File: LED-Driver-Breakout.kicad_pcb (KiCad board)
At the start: 6 copper layers, 120.9 x 67.1 mm, 16 parts, among them U1 V10P45-M3/86A, U2 TSR2-24120

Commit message: updates based on suggestions
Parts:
- added C3: 10µf, Capacitor_SMD:C_0805_2012Metric, F.Cu at (105.8, 109.2)
- added C4: 10µF, Capacitor_SMD:C_0805_2012Metric, F.Cu at (103.0, 109.2)
- added C5: 10µF, Capacitor_SMD:C_0805_2012Metric, F.Cu at (99.8, 109.5)
- added C6: 56µF, Capacitor_SMD:CP_Elec_8x10, F.Cu at (89.0, 112.2)
- added L1: 5.6µH, Inductor_SMD:L_0805_2012Metric_Pad1.05x1.20mm_HandSolder, F.Cu at (99.8, 112.2)
- moved U2 9.57 mm to (102.2, 118.8), turned to 0 degrees
- moved   1.40 mm to (100.6, 102.7)
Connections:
-   pad 1: V_Fused -> VRegulated
- PS1 pad 3: unconnected-(PS1-DIM--Pad3) -> GND
- PS1 pad 5: Switch pin -> Switch
- U2 pad 1: V_Fused -> Net-(U2-Vin)
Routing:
- net V_Fused: track 0.00 -> 41.6 mm, vias 6 -> 3
- net GND: track 0.00 -> 34.1 mm, vias 3 -> 4
- net Net-(U2-Vin): track 0.00 -> 23.5 mm
- net +BATT: track 23.0 -> 19.0 mm
- net (no net): track 0.00 -> 0.51 mm

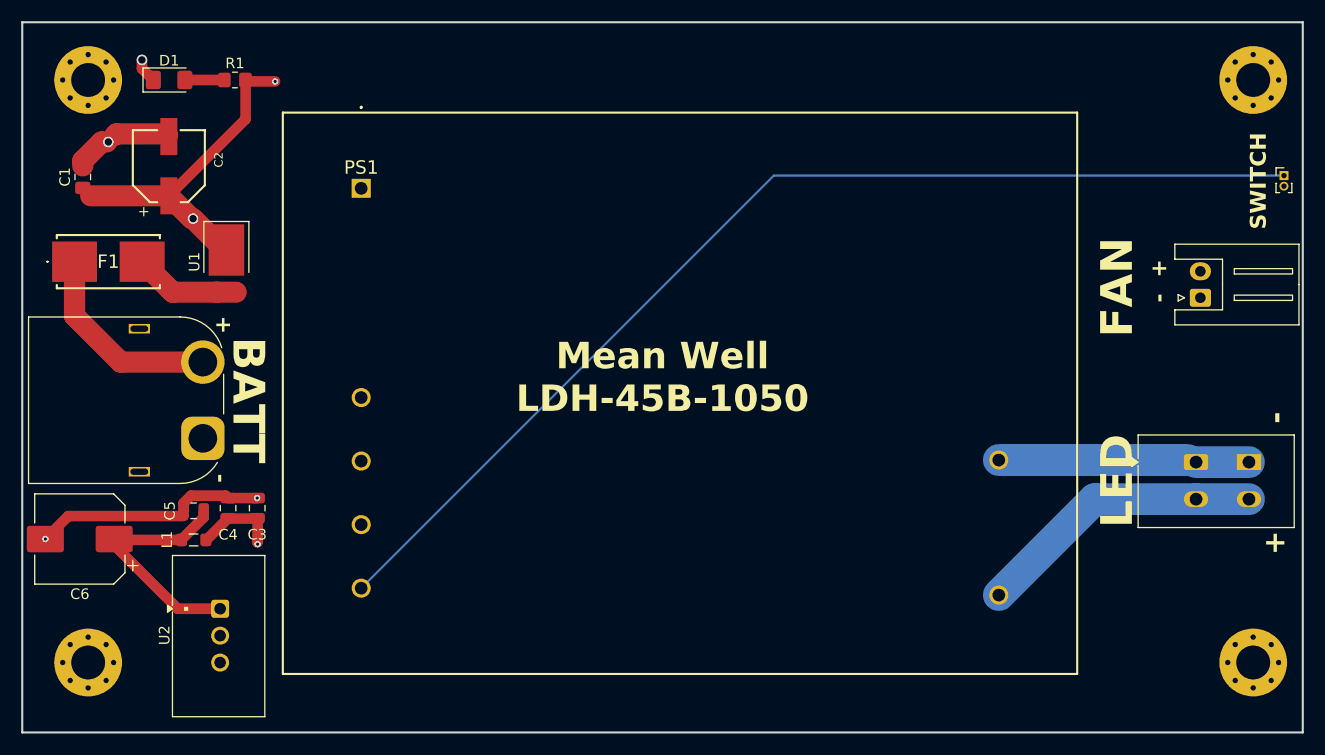
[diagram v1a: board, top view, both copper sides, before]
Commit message: finished pcb routing may need to make the board more square
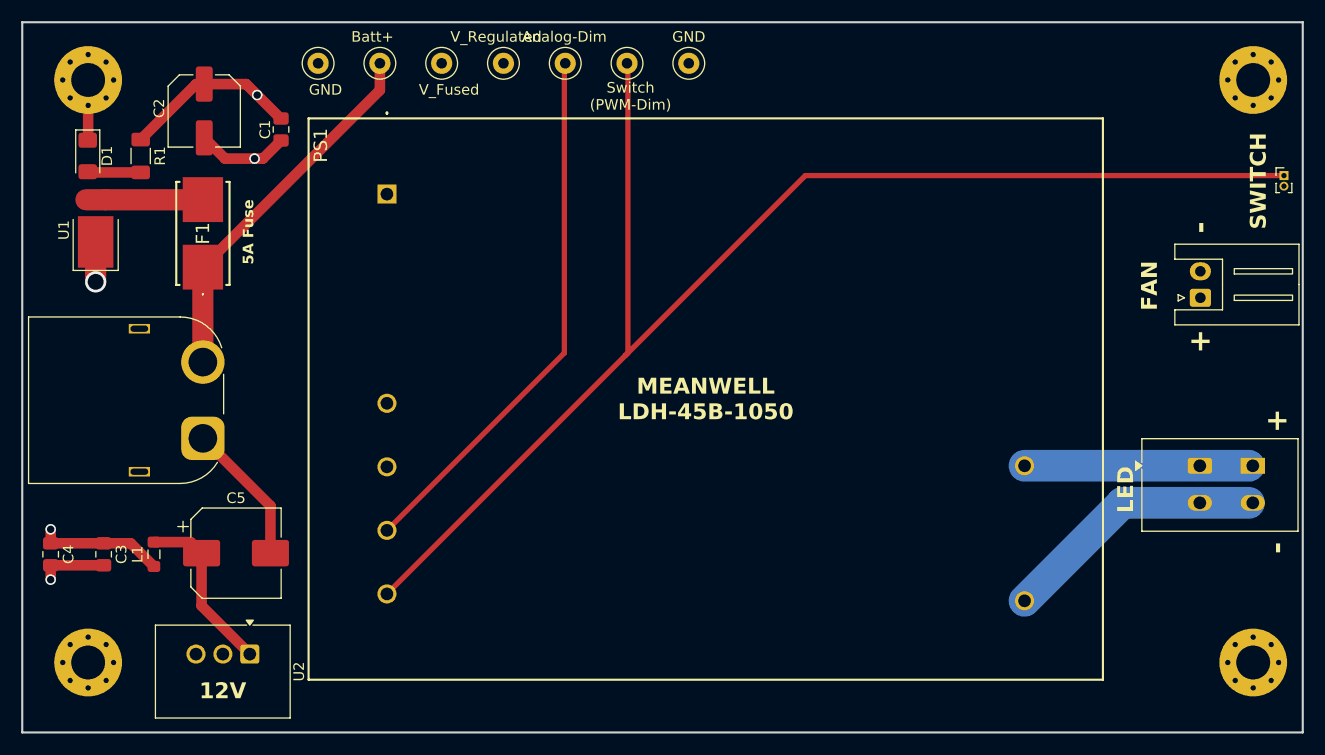
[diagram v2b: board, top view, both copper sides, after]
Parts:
- removed C6: 56µF, Capacitor_SMD:CP_Elec_8x10
- added Analog-Dim: TestPoint_Loop_D1.80mm_Drill1.0mm_Beaded, TestPoint:TestPoint_Loop_D1.80mm_Drill1.0mm_Beaded, F.Cu at (134.8, 67.2)
- added Batt+: TestPoint_Loop_D1.80mm_Drill1.0mm_Beaded, TestPoint:TestPoint_Loop_D1.80mm_Drill1.0mm_Beaded, F.Cu at (117.3, 67.2)
- added GND: TestPoint_Loop_D1.80mm_Drill1.0mm_Beaded, TestPoint:TestPoint_Loop_D1.80mm_Drill1.0mm_Beaded, F.Cu at (111.5, 67.2)
- added GND: TestPoint_Loop_D1.80mm_Drill1.0mm_Beaded, TestPoint:TestPoint_Loop_D1.80mm_Drill1.0mm_Beaded, F.Cu at (146.5, 67.2)
- added Switch(PWM-Dim): TestPoint_Loop_D1.80mm_Drill1.0mm_Beaded, TestPoint:TestPoint_Loop_D1.80mm_Drill1.0mm_Beaded, F.Cu at (140.7, 67.2)
- added V_Fused: TestPoint_Loop_D1.80mm_Drill1.0mm_Beaded, TestPoint:TestPoint_Loop_D1.80mm_Drill1.0mm_Beaded, F.Cu at (123.2, 67.2)
- added V_Regulated: TestPoint_Loop_D1.80mm_Drill1.0mm_Beaded, TestPoint:TestPoint_Loop_D1.80mm_Drill1.0mm_Beaded, F.Cu at (129.0, 67.2)
- C2: footprint 865080645012:WCAP-ASLI_6.3X7.7_DXL_ -> Capacitor_SMD:C_Elec_6.3x7.7
- C3: value 10µf -> 10 µF; footprint Capacitor_SMD:C_0805_2012Metric -> Capacitor_SMD:C_0805_2012Metric_Pad1.18x1.45mm_HandSolder
- C4: value 10µF -> 10 µF; footprint Capacitor_SMD:C_0805_2012Metric -> Capacitor_SMD:C_0805_2012Metric_Pad1.18x1.45mm_HandSolder
- C5: value 10µF -> 56 µF; footprint Capacitor_SMD:C_0805_2012Metric -> Capacitor_SMD:CP_Elec_8x10
- L1: value 5.6µH -> 5.6 µH
- R1: value 4.7 k -> 33K; footprint Resistor_SMD:R_0805_2012Metric_Pad1.20x1.40mm_HandSolder -> Resistor_SMD:R_1206_3216Metric_Pad1.30x1.75mm_HandSolder
- U2: value TSR2-24120 -> TSR0.5-2418; footprint Converter_DCDC:Converter_DCDC_TRACO_TSR2-xxxx_THT -> Converter_DCDC:Converter_DCDC_TRACO_TSR0.5-24xx_TSR0.5-24xxx_THT
- moved C1 19.2 mm to (108.0, 73.5), turned to -90 degrees
- moved C4 17.3 mm to (86.2, 113.6)
- moved C3 15.1 mm to (91.2, 113.6), turned to -90 degrees
- moved U1 12.7 mm to (90.5, 83.0), turned to 90 degrees
- moved R1 11.4 mm to (94.8, 76.0), turned to -90 degrees
- moved D1 10.5 mm to (89.8, 76.0), turned to -90 degrees
- moved F1 9.32 mm to (100.6, 83.3), turned to 90 degrees
- moved C2 6.19 mm to (100.8, 71.8)
- moved C5 5.66 mm to (103.8, 113.5), turned to 0 degrees
- moved U2 5.11 mm to (105.0, 123.0), turned to -90 degrees
- moved L1 3.99 mm to (96.0, 113.6), turned to 90 degrees
- moved PS1 2.49 mm to (118.0, 79.6)
- moved REF** 0.50 mm to (194.8, 105.2)
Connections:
- C4 pad 1: GND -> V_Fused
- C4 pad 2: V_Fused -> GND
- PS1 pad 5: Switch -> /switch
- REF** pad 1: Switch pin -> /switch
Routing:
- net /switch: track 0.00 -> 128.9 mm
- net Switch pin: track 103.3 -> 0.00 mm
- net unconnected-(PS1-ANALOG_DIM-Pad4): track 0.00 -> 51.1 mm
- net +BATT: track 19.0 -> 35.6 mm
- net V_Fused: track 41.6 -> 32.5 mm
- net Net-(U2-Vin): track 23.5 -> 16.3 mm
- net VOUT+: track 23.7 -> 21.2 mm
- net VOUT-: track 27.4 -> 25.0 mm
- net Net-(D1-A): track 3.73 -> 5.03 mm
- net Net-(F1-Pad2): track 10.1 -> 11.0 mm
- net (no net): track 0.51 -> 0.00 mm
- net GND: track 34.1 -> 34.3 mm, vias 4 -> 2
- added copper zone on In1.Cu, net GND
- removed copper zone on In1.Cu, net (none)
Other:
- board text added: "12V"
- board text added: "FAN"
- board text added: "MEANWELL LDH-45B-1050"
- board text added: "Switch (PWM-Dim)"
- board text removed: "."
- board text removed: "BATT"
- board text removed: "Mean Well LDH-45B-1050"

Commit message: forgot to save from last commit
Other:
- board text added: "45W LED Driver Breakout"

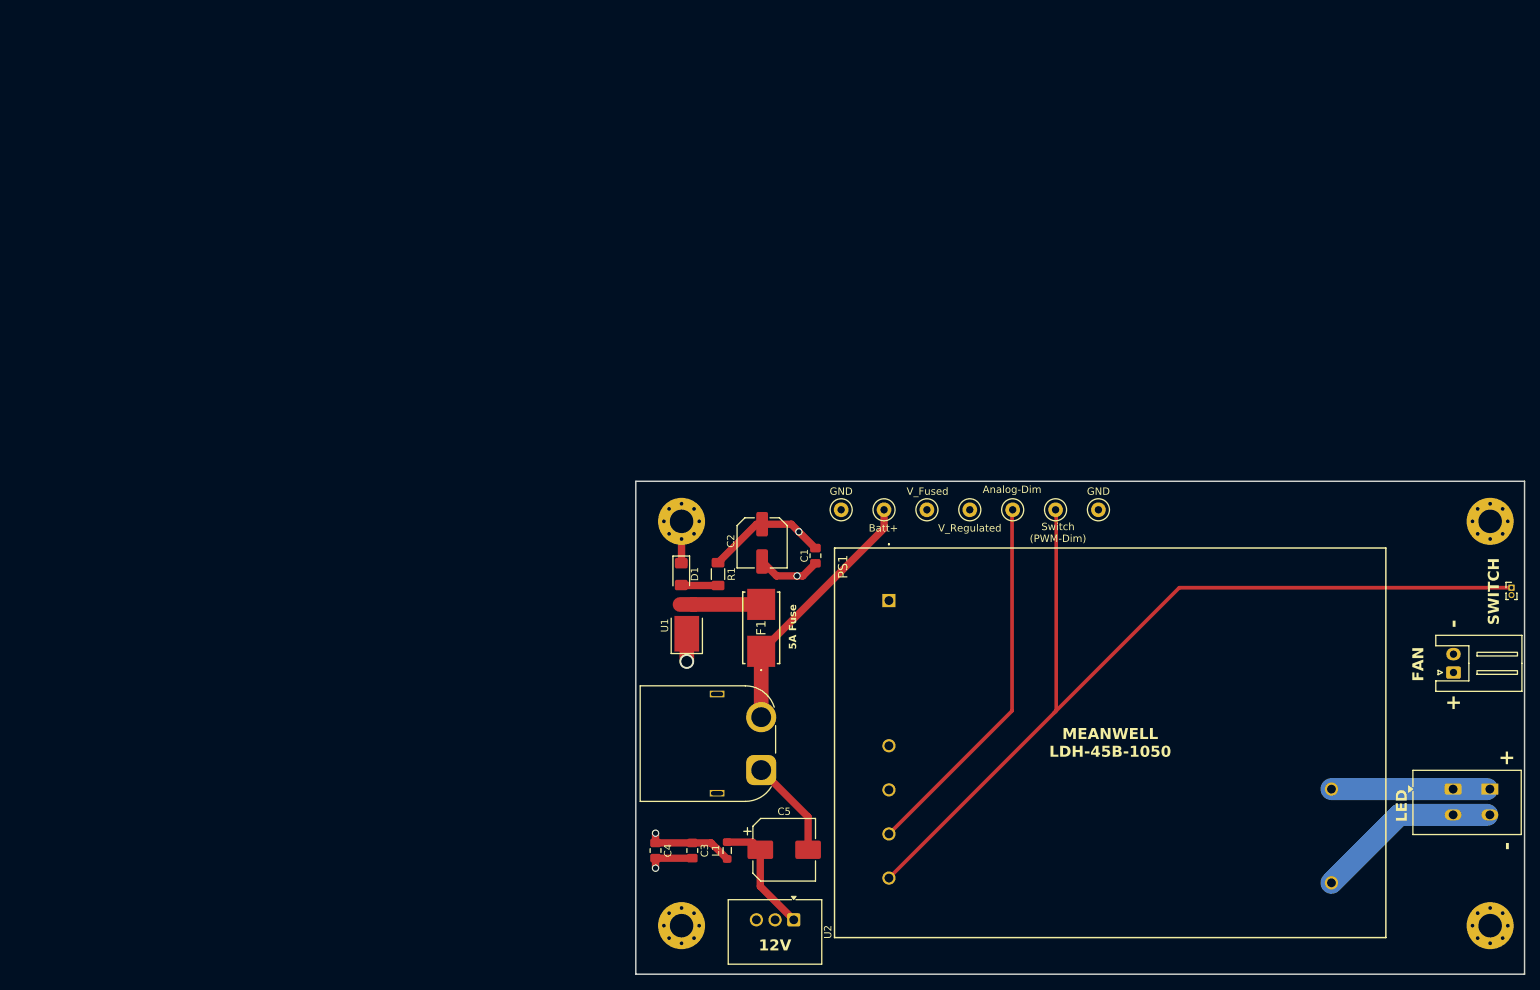
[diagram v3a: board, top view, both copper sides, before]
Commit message: made board square only need to add graphics
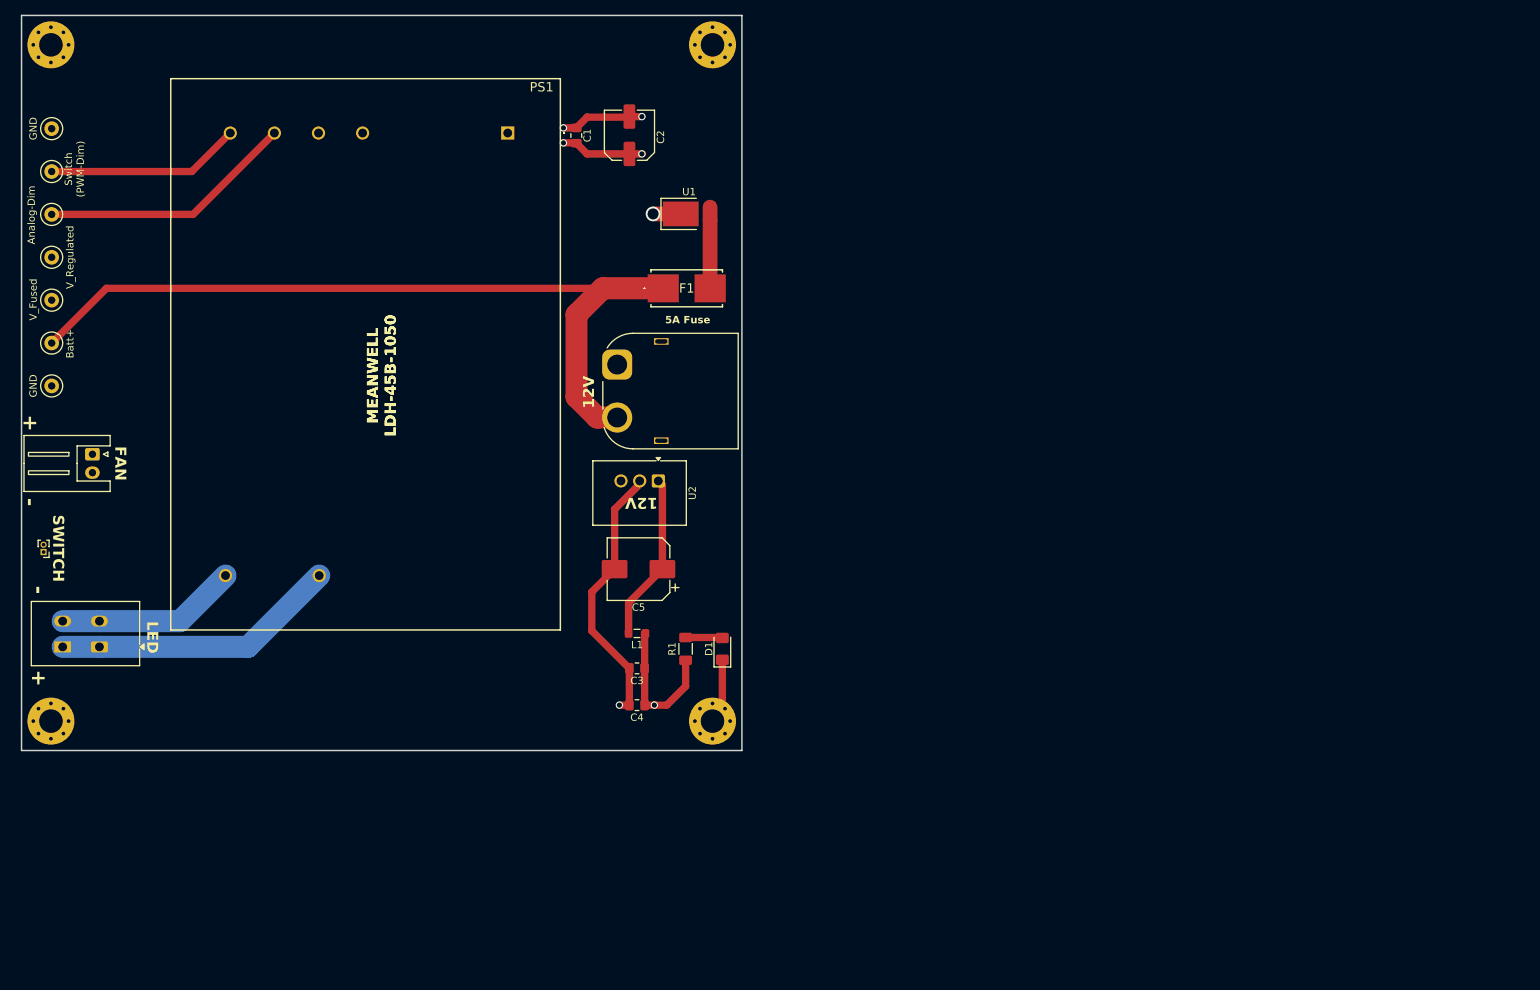
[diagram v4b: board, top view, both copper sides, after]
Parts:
- moved REF** 199.8 mm to (3.00, 73.0), turned to 180 degrees
- moved   187.5 mm to (9.64, 59.7), turned to -90 degrees
- moved REF** 185.2 mm to (10.6, 85.9), turned to 90 degrees
- moved GND 151.5 mm to (4.10, 15.4), turned to 90 degrees
- moved Switch(PWM-Dim) 144.1 mm to (4.10, 21.2), turned to 90 degrees
- moved Analog-Dim 136.8 mm to (4.10, 27.1), turned to -90 degrees
- moved V_Regulated 129.5 mm to (4.10, 32.9), turned to -90 degrees
- moved   124.1 mm to (94.0, 4.00)
- moved V_Fused 122.4 mm to (4.10, 38.7), turned to 90 degrees
- moved Batt+ 115.5 mm to (4.10, 44.6), turned to -90 degrees
- moved   109.4 mm to (94.0, 96.0)
- moved GND 108.7 mm to (4.10, 50.4), turned to 90 degrees
- moved   107.5 mm to (4.00, 4.00)
- moved   90.2 mm to (4.00, 96.0)
- moved PS1 82.1 mm to (66.2, 16.0), turned to 180 degrees
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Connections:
- REF** pad 1: /switch -> (no net)
- REF** pad 2: GND -> (no net)
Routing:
- net /switch: track 128.9 -> 26.8 mm
- net +BATT: track 35.6 -> 117.5 mm
- net GND: track 34.3 -> 57.1 mm, vias 2 -> 3
- net VOUT+: track 21.2 -> 38.9 mm
- net unconnected-(PS1-ANALOG_DIM-Pad4): track 51.1 -> 35.0 mm
- net Net-(U2-Vin): track 16.3 -> 22.9 mm
- net V_Fused: track 32.5 -> 35.1 mm, vias 3 -> 4
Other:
- board size 120.9 x 67.1 mm -> 98 x 100 mm

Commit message: forgot to add switch trace
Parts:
- moved U2 84.0 mm to (154.7, 112.5)
- moved   83.8 mm to (77.5, 108.8)
- moved Analog-Dim 83.5 mm to (71.6, 76.3)
- moved D1 83.5 mm to (162.9, 135.4)
- moved R1 83.5 mm to (157.9, 135.4)
- moved Switch(PWM-Dim) 83.5 mm to (71.6, 70.4)
- moved V_Fused 83.5 mm to (71.6, 87.9)
- moved   83.5 mm to (161.5, 53.2)
- moved   83.5 mm to (161.5, 145.2)
- moved Batt+ 83.5 mm to (71.6, 93.8)
- moved C1 83.5 mm to (143.0, 65.5)
- moved C5 83.5 mm to (151.5, 124.5)
- moved GND 83.5 mm to (71.6, 99.6)
- moved GND 83.5 mm to (71.6, 64.6)
- moved REF** 83.5 mm to (78.1, 135.1)
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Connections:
- REF** pad 1: (no net) -> /switch
- REF** pad 2: (no net) -> GND
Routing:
- net /switch: track 26.8 -> 79.2 mm

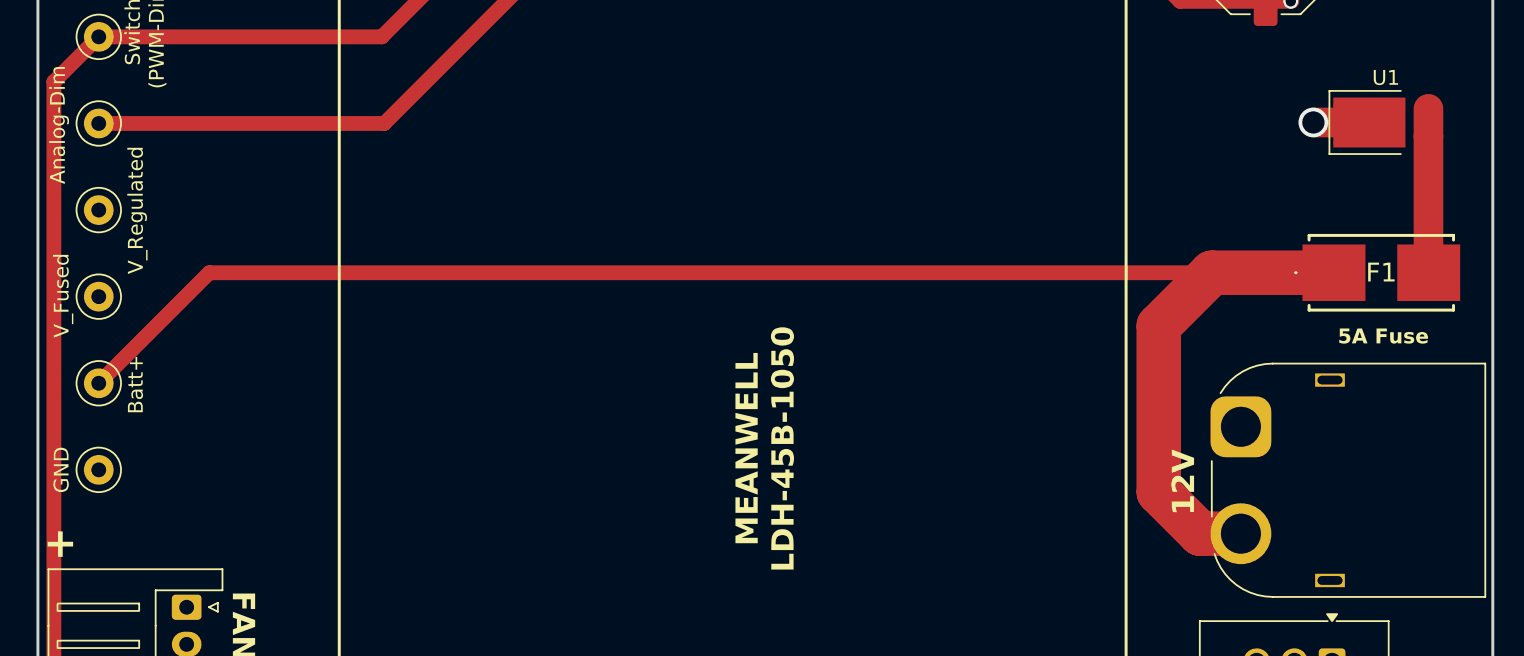
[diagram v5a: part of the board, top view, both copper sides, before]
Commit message: Updates trace widths; now realizing the regulator on the schematic is improperly labeled and test points need to be properly made.
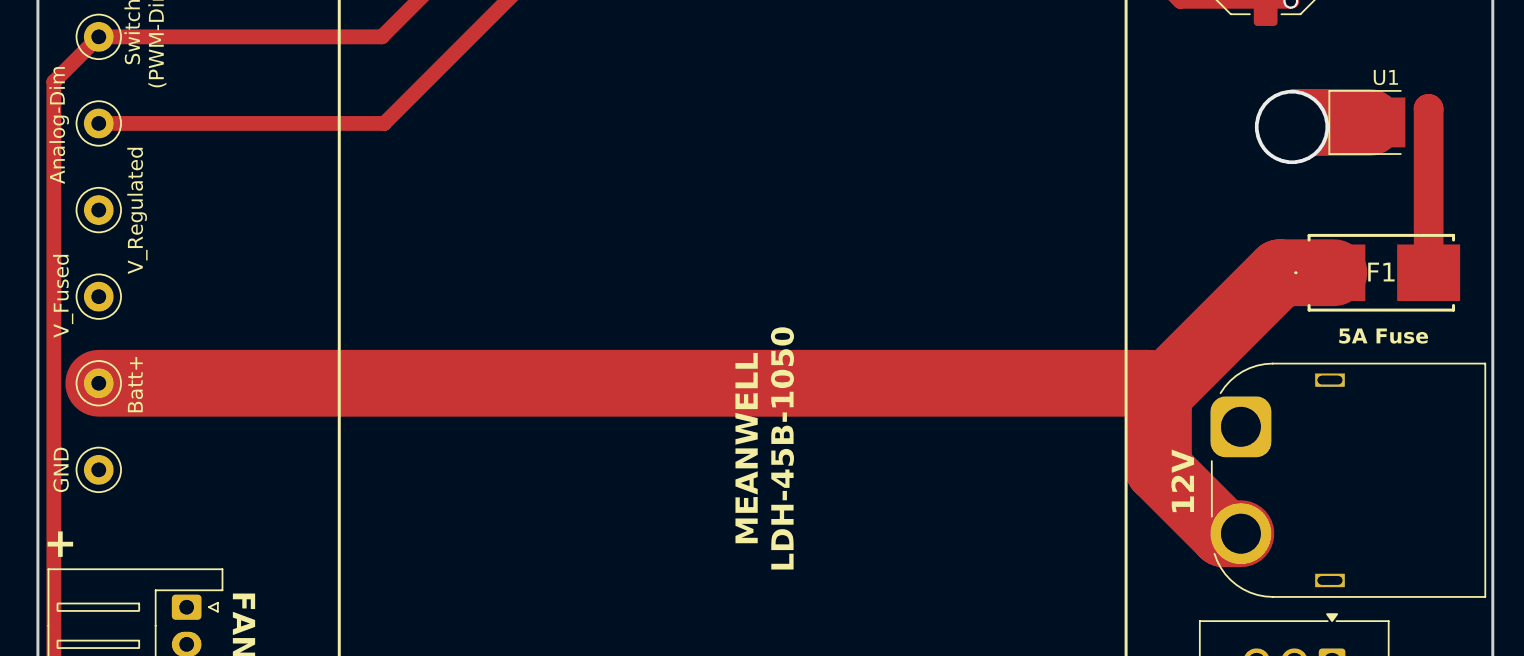
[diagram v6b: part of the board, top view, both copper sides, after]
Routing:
- net +BATT: track 117.5 -> 99.4 mm
- net V_Fused: track 35.1 -> 36.7 mm
